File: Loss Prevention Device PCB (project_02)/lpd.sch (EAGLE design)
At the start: 0 parts

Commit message: Schematic'ed all parts but the usb
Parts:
- added K1: LPPB041NGCN-RC, lpd:LPPB041NGCN-RC
- added U1: POCKETBEAGLE, lpd:POCKETBEAGLE
- added U2: GT-U7, lpd:GT-U7
- added U3: HM-10, lpd:HM-10
- added X1: (no value), lpd:GHI2_USB_HOST_W/CHASSIS_GND
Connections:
- new net ANGLE1: K1.P$5, U3.VCC
- new net ANGLE2: K1.P$6, U3.GND
- new net ANGLE3: K1.P$7, U3.TXD
- new net ANGLE4: K1.P$8, U3.RXD
- new net GND: K1.P$2, U1.GND@2, U1.GND@3, U1.GND@4, U1.GND@5, U2.GND
- new net UART2.RX: U1.SPI0.CLK, U2.RXD
- new net UART2.TX: U1.SPI0.MISO, U2.TXD
- new net UART4.RX: K1.P$4, U1.UART4.RX
- new net UART4.TX: K1.P$3, U1.UART4.TX
- new net VDD_3P3V: K1.P$1, U1.3.3V@1, U1.3.3V@2, U2.VCC
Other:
- note added: "90 Degree Female Header"
- note added: "Bluetooth Module"
- note added: "GPS"
- note added: "PocketBeagle"
- note added: "USB"

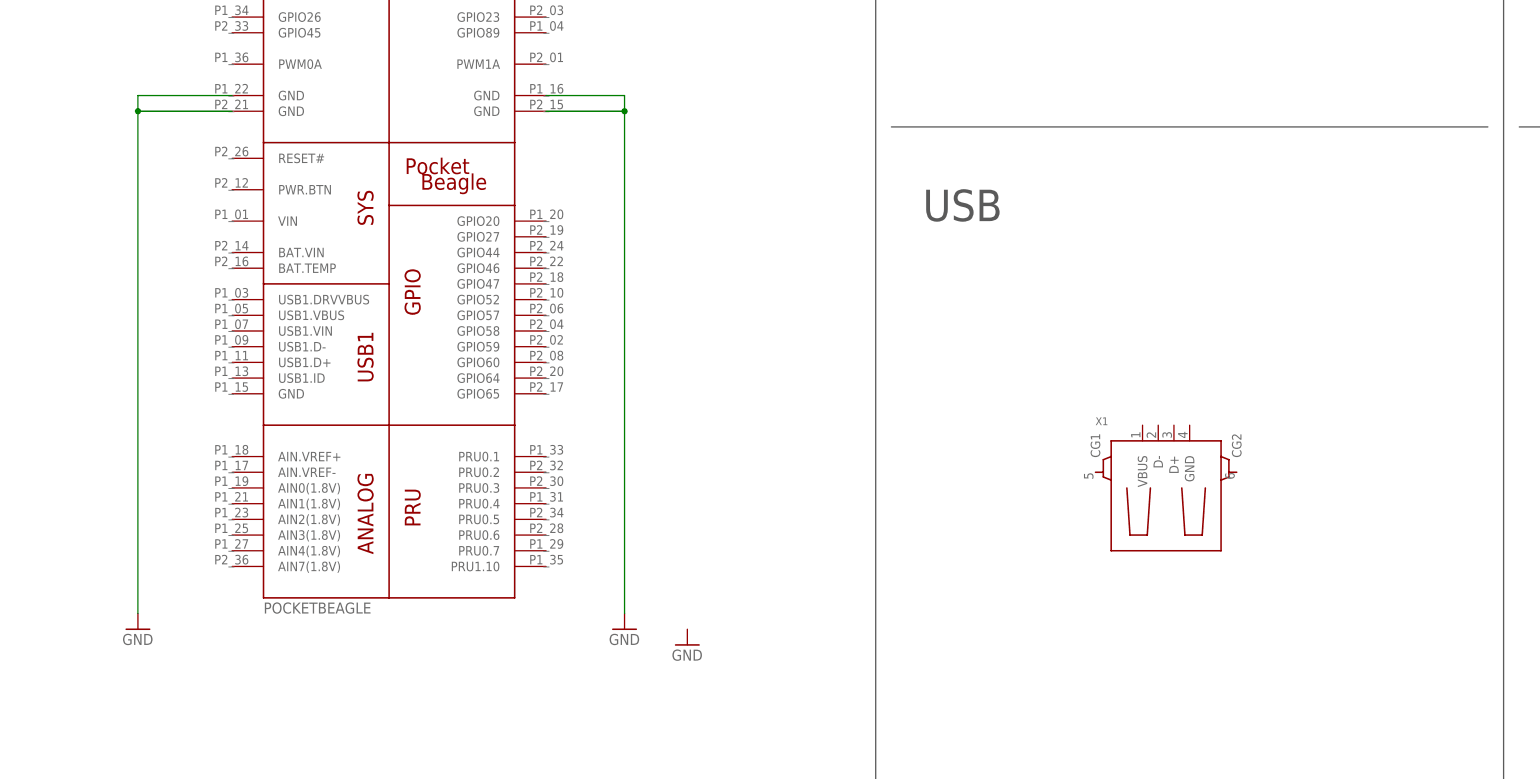
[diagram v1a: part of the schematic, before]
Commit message: Added USB connections
For some reason when I imported the CGND part to my LPD library my schematic couldn't read from it anymore...
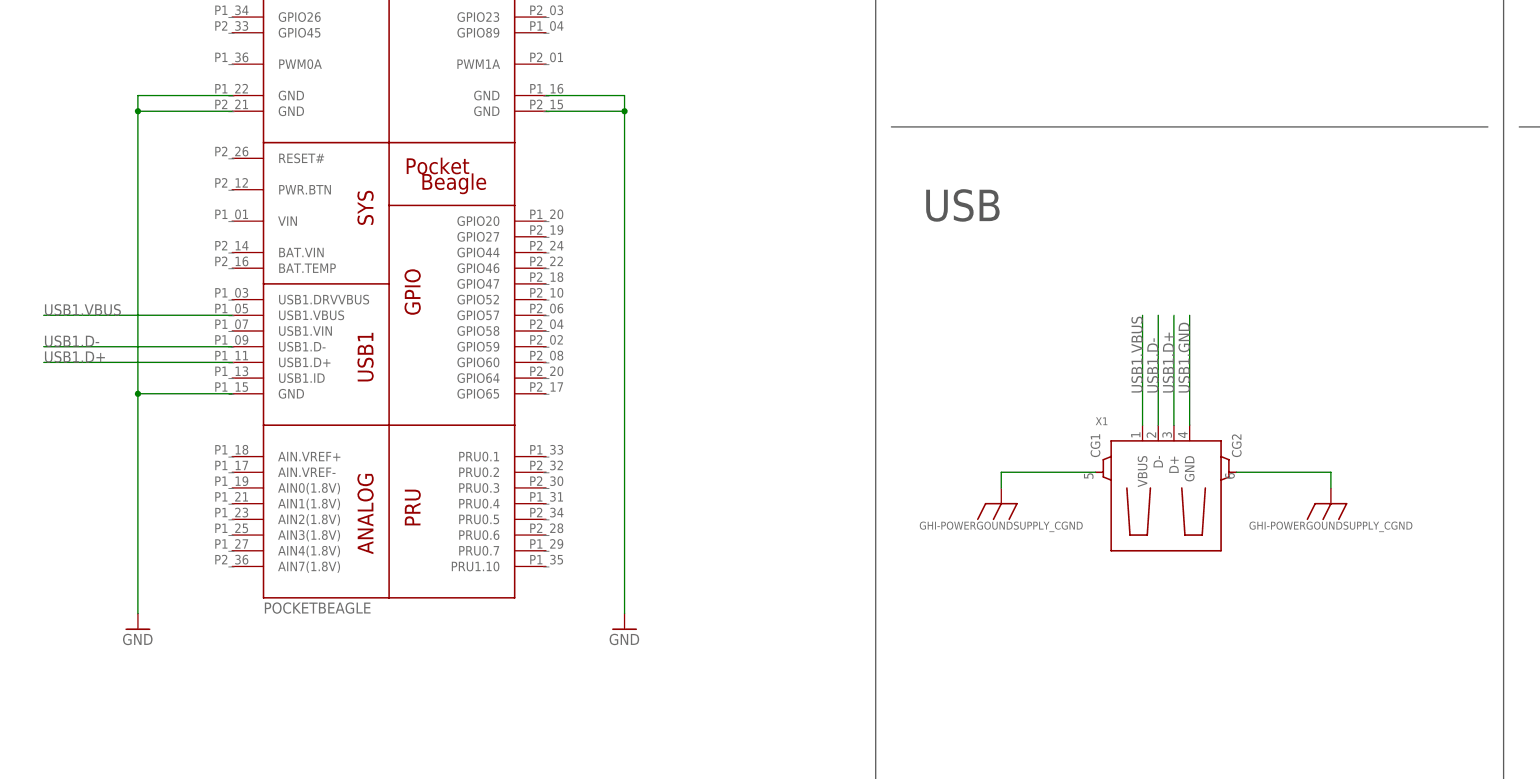
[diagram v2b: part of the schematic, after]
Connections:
- new net CGND: X1.CG1, X1.CG2
- new net USB1.D+: U1.USB1.D+, X1.D+
- new net USB1.D-: U1.USB1.D-, X1.D-
- new net USB1.GND: X1.GND
- new net USB1.VBUS: U1.USB1.VBUS, X1.VBUS
- net GND: now also U1.GND@1
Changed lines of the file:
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@@
 <part name="SUPPLY2" library="ENGI301" deviceset="VDD_3P3V" device=""/>
 <part name="GND2" library="ENGI301" deviceset="GND" device=""/>
-<part name="GND3" library="ENGI301" deviceset="GND" device=""/>
 <part name="SUPPLY3" library="lpd" deviceset="VDD_3P3V" device=""/>
 <part name="GND4" library="lpd" deviceset="GND" device=""/>
 <part name="GND5" library="lpd" deviceset="GND" device=""/>
 <part name="SUPPLY4" library="lpd" deviceset="VDD_3P3V" device=""/>
+<part name="SUPPLY5" library="BeagleBone_Blue" deviceset="GHI-POWERGOUNDSUPPLY_CGND" device=""/>
+<part name="SUPPLY6" library="BeagleBone_Blue" deviceset="GHI-POWERGOUNDSUPPLY_CGND" device=""/>
 </parts>
 <sheets>
@@
 <attribute name="VALUE" x="33.02" y="58.42" size="1.778" layer="96"/>
 </instance>
-<instance part="GND3" gate="1" x="124.46" y="58.42" smashed="yes">
-<attribute name="VALUE" x="121.92" y="55.88" size="1.778" layer="96"/>
-</instance>
 <instance part="SUPPLY3" gate="G$1" x="223.52" y="190.5" smashed="yes">
 <attribute name="VALUE" x="223.52" y="194.564" size="1.778" layer="96" align="center"/>
@@
 <instance part="SUPPLY4" gate="G$1" x="302.26" y="71.12" smashed="yes">
 <attribute name="VALUE" x="302.26" y="75.184" size="1.778" layer="96" align="center"/>
+</instance>
+<instance part="SUPPLY5" gate="G$1" x="175.26" y="81.28" smashed="yes">
+<attribute name="VALUE" x="175.26" y="77.724" size="1.27" layer="96" align="center"/>
+</instance>
+<instance part="SUPPLY6" gate="G$1" x="228.6" y="81.28" smashed="yes">
+<attribute name="VALUE" x="228.6" y="77.724" size="1.27" layer="96" align="center"/>
 </instance>
 </instances>
@@
 <wire x1="35.56" y1="147.32" x2="35.56" y2="144.78" width="0.1524" layer="91"/>
 <pinref part="U1" gate="G$1" pin="GND@5"/>
-<wire x1="35.56" y1="144.78" x2="35.56" y2="63.5" width="0.1524" layer="91"/>
+<wire x1="35.56" y1="144.78" x2="35.56" y2="99.06" width="0.1524" layer="91"/>
+<wire x1="35.56" y1="99.06" x2="35.56" y2="63.5" width="0.1524" layer="91"/>
 <wire x1="50.8" y1="144.78" x2="35.56" y2="144.78" width="0.1524" layer="91"/>
 <junction x="35.56" y="144.78"/>
+<pinref part="U1" gate="G$1" pin="GND@1"/>
+<wire x1="50.8" y1="99.06" x2="35.56" y2="99.06" width="0.1524" layer="91"/>
+<junction x="35.56" y="99.06"/>
 </segment>
 <segment>
@@
 </segment>
 </net>
+<net name="CGND" class="0">
+<segment>
+<pinref part="X1" gate="G$1" pin="CG1"/>
+<pinref part="SUPPLY5" gate="G$1" pin="CGND"/>
+<wire x1="190.5" y1="86.36" x2="175.26" y2="86.36" width="0.1524" layer="91"/>
+<wire x1="175.26" y1="86.36" x2="175.26" y2="83.82" width="0.1524" layer="91"/>
+</segment>
+<segment>
+<pinref part="SUPPLY6" gate="G$1" pin="CGND"/>
+<pinref part="X1" gate="G$1" pin="CG2"/>
+<wire x1="228.6" y1="83.82" x2="228.6" y2="86.36" width="0.1524" layer="91"/>
+<wire x1="228.6" y1="86.36" x2="213.36" y2="86.36" width="0.1524" layer="91"/>
+</segment>
+</net>
+<net name="USB1.VBUS" class="0">
+<segment>
+<pinref part="X1" gate="G$1" pin="VBUS"/>
+<wire x1="198.12" y1="93.98" x2="198.12" y2="111.76" width="0.1524" layer="91"/>
+<label x="198.12" y="99.06" size="1.778" layer="95" rot="R90"/>
+</segment>
+<segment>
+<pinref part="U1" gate="G$1" pin="USB1.VBUS"/>
+<wire x1="50.8" y1="111.76" x2="20.32" y2="111.76" width="0.1524" layer="91"/>
+<label x="20.32" y="111.76" size="1.778" layer="95"/>
+</segment>
+</net>
+<net name="USB1.D-" class="0">
+<segment>
+<pinref part="X1" gate="G$1" pin="D-"/>
+<wire x1="200.66" y1="93.98" x2="200.66" y2="111.76" width="0.1524" layer="91"/>
+<label x="200.66" y="99.06" size="1.778" layer="95" rot="R90"/>
+</segment>
+<segment>
+<pinref part="U1" gate="G$1" pin="USB1.D-"/>
+<wire x1="50.8" y1="106.68" x2="20.32" y2="106.68" width="0.1524" layer="91"/>
+<label x="20.32" y="106.68" size="1.778" layer="95"/>
+</segment>
+</net>
+<net name="USB1.D+" class="0">
+<segment>
+<pinref part="X1" gate="G$1" pin="D+"/>
+<wire x1="203.2" y1="93.98" x2="203.2" y2="111.76" width="0.1524" layer="91"/>
+<label x="203.2" y="99.06" size="1.778" layer="95" rot="R90"/>
+</segment>
+<segment>
+<pinref part="U1" gate="G$1" pin="USB1.D+"/>
+<wire x1="50.8" y1="104.14" x2="20.32" y2="104.14" width="0.1524" layer="91"/>
+<label x="20.32" y="104.14" size="1.778" layer="95"/>
+</segment>
+</net>
+<net name="USB1.GND" class="0">
+<segment>
+<pinref part="X1" gate="G$1" pin="GND"/>
+<wire x1="205.74" y1="93.98" x2="205.74" y2="111.76" width="0.1524" layer="91"/>
+<label x="205.74" y="99.06" size="1.778" layer="95" rot="R90"/>
+</segment>
+</net>

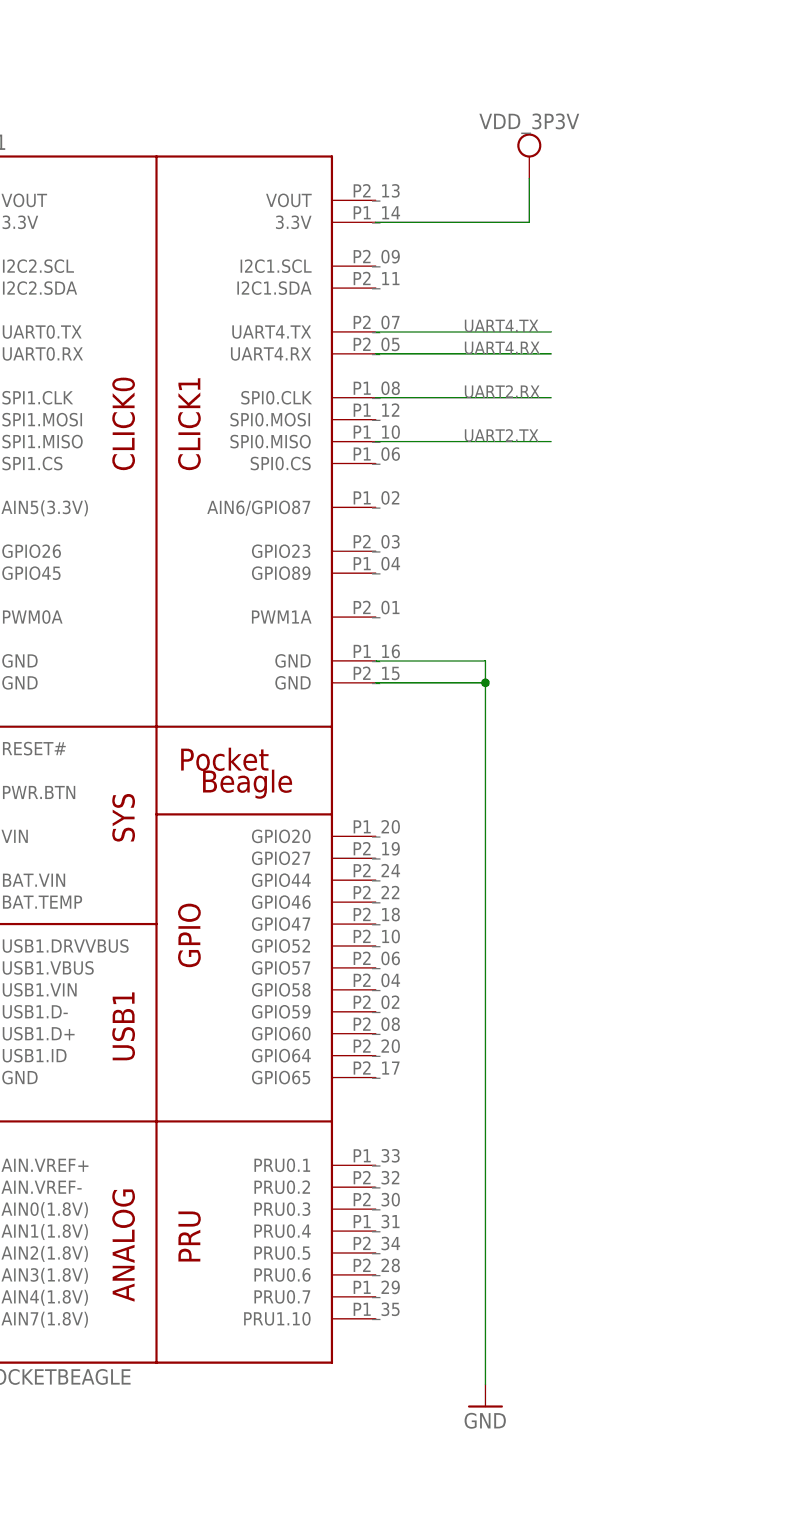
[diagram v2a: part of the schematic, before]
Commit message: Updated PocketBeagle Symbol/Footprint
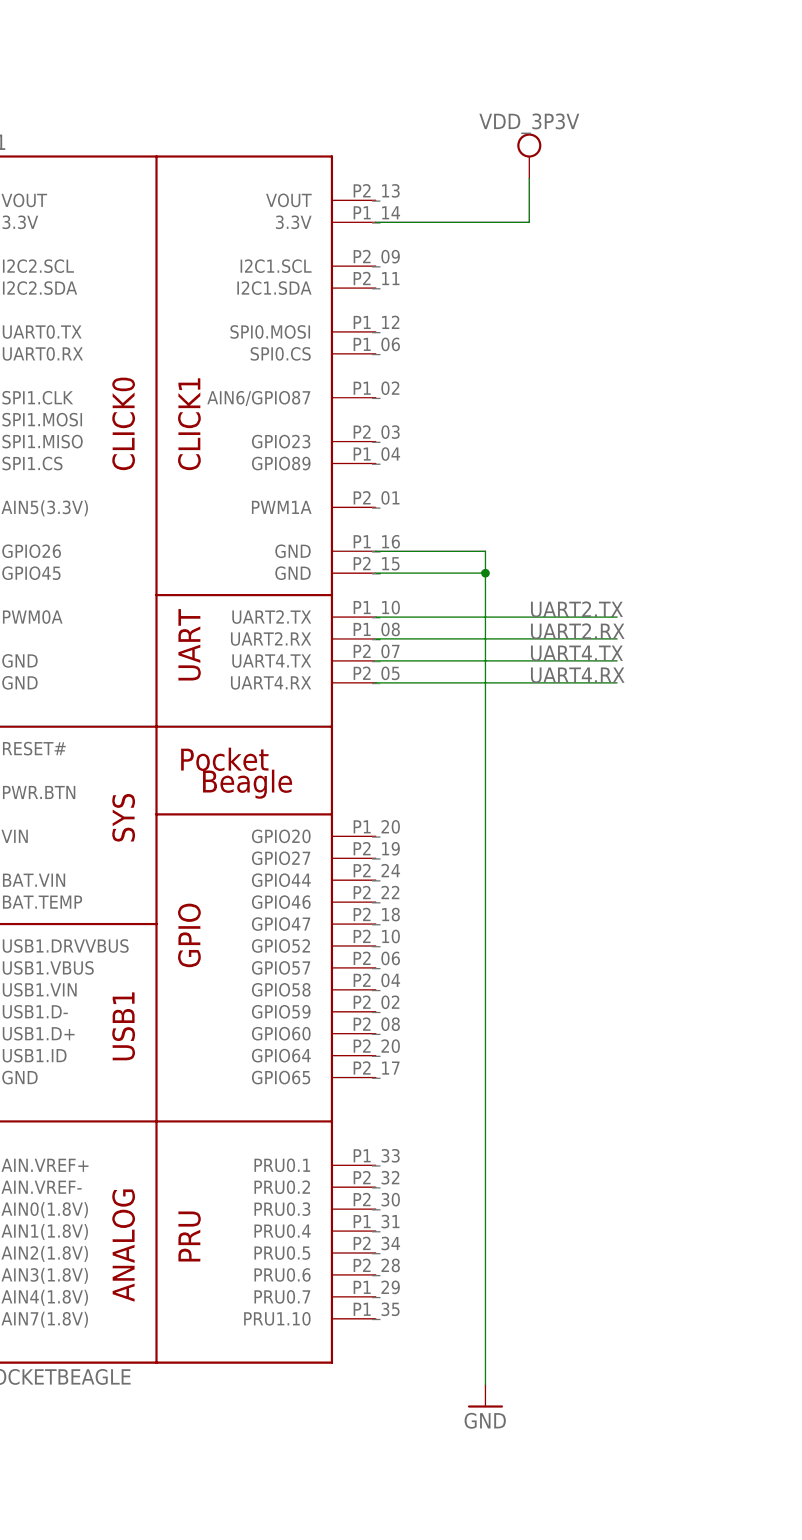
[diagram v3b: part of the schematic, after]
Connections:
- net UART2.RX: now also U1.UART2.RX; no longer U1.SPI0.CLK
- net UART2.TX: now also U1.UART2.TX; no longer U1.SPI0.MISO
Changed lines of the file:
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@@
 <net name="GND" class="0">
-<segment>
-<pinref part="U1" gate="G$1" pin="GND@2"/>
-<pinref part="GND1" gate="1" pin="GND"/>
-<wire x1="101.6" y1="147.32" x2="114.3" y2="147.32" width="0.1524" layer="91"/>
-<wire x1="114.3" y1="147.32" x2="114.3" y2="144.78" width="0.1524" layer="91"/>
-<pinref part="U1" gate="G$1" pin="GND@4"/>
-<wire x1="114.3" y1="144.78" x2="114.3" y2="63.5" width="0.1524" layer="91"/>
-<wire x1="101.6" y1="144.78" x2="114.3" y2="144.78" width="0.1524" layer="91"/>
-<junction x="114.3" y="144.78"/>
-</segment>
 <segment>
 <pinref part="U1" gate="G$1" pin="GND@3"/>
@@
 <wire x1="317.5" y1="86.36" x2="317.5" y2="60.96" width="0.1524" layer="91"/>
 </segment>
+<segment>
+<pinref part="U1" gate="G$1" pin="GND@2"/>
+<pinref part="GND1" gate="1" pin="GND"/>
+<wire x1="101.6" y1="160.02" x2="114.3" y2="160.02" width="0.1524" layer="91"/>
+<wire x1="114.3" y1="160.02" x2="114.3" y2="157.48" width="0.1524" layer="91"/>
+<pinref part="U1" gate="G$1" pin="GND@4"/>
+<wire x1="114.3" y1="157.48" x2="114.3" y2="63.5" width="0.1524" layer="91"/>
+<wire x1="101.6" y1="157.48" x2="114.3" y2="157.48" width="0.1524" layer="91"/>
+<junction x="114.3" y="157.48"/>
+</segment>
 </net>
 <net name="UART2.RX" class="0">
-<segment>
-<pinref part="U1" gate="G$1" pin="SPI0.CLK"/>
-<wire x1="101.6" y1="177.8" x2="121.92" y2="177.8" width="0.1524" layer="91"/>
-<label x="111.76" y="177.8" size="1.4224" layer="95" font="vector"/>
-</segment>
 <segment>
 <pinref part="U2" gate="G$1" pin="RXD"/>
@@
 <label x="205.74" y="177.8" size="1.27" layer="95" font="vector" rot="R90"/>
 </segment>
+<segment>
+<pinref part="U1" gate="G$1" pin="UART2.RX"/>
+<wire x1="101.6" y1="149.86" x2="129.54" y2="149.86" width="0.1524" layer="91"/>
+<label x="119.38" y="149.86" size="1.778" layer="95"/>
+</segment>
 </net>
 <net name="UART2.TX" class="0">
-<segment>
-<pinref part="U1" gate="G$1" pin="SPI0.MISO"/>
-<wire x1="101.6" y1="172.72" x2="121.92" y2="172.72" width="0.1524" layer="91"/>
-<label x="111.76" y="172.72" size="1.4224" layer="95" font="vector"/>
-</segment>
 <segment>
 <pinref part="U2" gate="G$1" pin="TXD"/>
@@
 <label x="203.2" y="177.8" size="1.27" layer="95" font="vector" rot="R90"/>
 </segment>
+<segment>
+<pinref part="U1" gate="G$1" pin="UART2.TX"/>
+<wire x1="101.6" y1="152.4" x2="129.54" y2="152.4" width="0.1524" layer="91"/>
+<label x="119.38" y="152.4" size="1.778" layer="95"/>
+</segment>
 </net>
 <net name="UART4.TX" class="0">
-<segment>
-<pinref part="U1" gate="G$1" pin="UART4.TX"/>
-<wire x1="101.6" y1="185.42" x2="121.92" y2="185.42" width="0.1524" layer="91"/>
-<label x="111.76" y="185.42" size="1.4224" layer="95" font="vector"/>
-</segment>
 <segment>
 <pinref part="K1" gate="G$1" pin="P$3"/>
@@
 <label x="320.04" y="63.5" size="1.4224" layer="95" font="vector" rot="R90"/>
 </segment>
+<segment>
+<pinref part="U1" gate="G$1" pin="UART4.TX"/>
+<wire x1="101.6" y1="147.32" x2="129.54" y2="147.32" width="0.1524" layer="91"/>
+<label x="119.38" y="147.32" size="1.778" layer="95"/>
+</segment>
 </net>
 <net name="UART4.RX" class="0">
-<segment>
-<pinref part="U1" gate="G$1" pin="UART4.RX"/>
-<wire x1="101.6" y1="182.88" x2="121.92" y2="182.88" width="0.1524" layer="91"/>
-<label x="111.76" y="182.88" size="1.4224" layer="95" font="vector"/>
-</segment>
 <segment>
 <pinref part="K1" gate="G$1" pin="P$4"/>
@@
 <label x="322.58" y="63.5" size="1.4224" layer="95" font="vector" rot="R90"/>
 </segment>
+<segment>
+<pinref part="U1" gate="G$1" pin="UART4.RX"/>
+<wire x1="101.6" y1="144.78" x2="129.54" y2="144.78" width="0.1524" layer="91"/>
+<label x="119.38" y="144.78" size="1.778" layer="95"/>
+</segment>
 </net>

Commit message: Split pocketbeagle symbol into 2
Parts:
- removed U1: POCKETBEAGLE, lpd:POCKETBEAGLE
- added U$1: POCKETBEAGLE, lpd:POCKETBEAGLE
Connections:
- removed net USB1.GND: X1.GND
- net GND: now also U$1G$2.GND@1, U$1G$2.GND@2, U$1G$2.GND@3, U$1G$2.GND@4, U$1G$2.GND@5, X1.GND; no longer U1.GND@1, U1.GND@2, U1.GND@3, U1.GND@4, U1.GND@5
- net UART2.RX: now also U$1G$2.UART2.RX; no longer U1.UART2.RX
- net UART2.TX: now also U$1G$2.UART2.TX; no longer U1.UART2.TX
- net UART4.RX: now also U$1G$2.UART4.RX; no longer U1.UART4.RX
- net UART4.TX: now also U$1G$2.UART4.TX; no longer U1.UART4.TX
- net USB1.D+: now also U$1G$2.USB1.D+; no longer U1.USB1.D+
- net USB1.D-: now also U$1G$2.USB1.D-; no longer U1.USB1.D-
- net USB1.VBUS: now also U$1G$2.USB1.VBUS; no longer U1.USB1.VBUS
- net VDD_3P3V: now also U$1G$2.3.3V@1, U$1G$2.3.3V@2; no longer U1.3.3V@1, U1.3.3V@2
